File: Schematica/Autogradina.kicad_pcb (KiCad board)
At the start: 2 copper layers, 100 x 100 mm, 50 parts, among them J1 Power_Connector, J2 AC_Connector, J3 UART_Connector, J4 USB_B_Micro, J5 Boot_Jumper, J6 Ports_Connector, J7 Conn_01x02_Socket, J8 Conn_01x02_Socket, J9 Conn_01x02_Socket, K1 G5LE-1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

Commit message: Improvements
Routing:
- net 3.3V: track 0.00 -> 90.3 mm
- net N_To_Ground_Probe: track 0.00 -> 83.4 mm, vias 0 -> 2
- net Net-(U2-EN): track 0.00 -> 36.7 mm, vias 0 -> 2
- net Net-(J5-Pin_2): track 0.00 -> 18.9 mm
- net RELAY1_CONTROL: track 0.00 -> 12.1 mm, vias 0 -> 2
- net RELAY3_CONTROL: track 0.00 -> 7.98 mm
- net Net-(J4-D+): track 0.00 -> 7.47 mm
- net RELAY2_CONTROL: track 0.00 -> 7.26 mm
- net Net-(J4-D-): track 0.00 -> 7.21 mm
- net Net-(D7-A): track 7.66 -> 8.65 mm
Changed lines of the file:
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@@
   (gr_rect (start 28 27) (end 128 127)
     (stroke (width 0.1) (type default)) (fill none) (layer "Edge.Cuts"))
+  (segment (start 82.995 33.95) (end 79.405 37.54) (width 0.5) (layer "F.Cu") (net 1))
+  (segment (start 40.64 71.12) (end 33.02 63.5) (width 0.35) (layer "F.Cu") (net 1))
+  (segment (start 120.45 33.95) (end 82.995 33.95) (width 0.5) (layer "F.Cu") (net 1))
+  (segment (start 122 35.5) (end 120.45 33.95) (width 0.5) (layer "F.Cu") (net 1))
+  (segment (start 40.64 93.82) (end 40.64 71.12) (width 0.35) (layer "F.Cu") (net 1))
+  (segment (start 79.405 37.54) (end 73.08 43.865) (width 0.5) (layer "F.Cu") (net 1))
+  (segment (start 73.08 43.865) (end 73.08 47) (width 0.5) (layer "F.Cu") (net 1))
   (segment (start 63.75 28.75) (end 63.71 28.71) (width 2) (layer "F.Cu") (net 2))
   (segment (start 67 82.08) (end 70 82.08) (width 0.25) (layer "F.Cu") (net 2))
@@
   (segment (start 61 82.08) (end 64 82.08) (width 0.25) (layer "F.Cu") (net 2))
   (segment (start 89 57.08) (end 96.92 57.08) (width 2) (layer "F.Cu") (net 2))
+  (segment (start 63.75 33.25) (end 61.25 33.25) (width 0.5) (layer "F.Cu") (net 3))
+  (segment (start 62.92 41.08) (end 63 41) (width 0.5) (layer "F.Cu") (net 3))
+  (segment (start 62.92 47) (end 62.92 41.08) (width 0.5) (layer "F.Cu") (net 3))
+  (segment (start 40.52 32) (end 40.25 31.73) (width 0.5) (layer "F.Cu") (net 3))
+  (segment (start 43 32) (end 40.52 32) (width 0.5) (layer "F.Cu") (net 3))
+  (segment (start 70.25 33.25) (end 63.75 33.25) (width 0.5) (layer "F.Cu") (net 3))
+  (segment (start 61.25 33.25) (end 61 33) (width 0.5) (layer "F.Cu") (net 3))
+  (via (at 43 32) (size 0.8) (drill 0.4) (layers "F.Cu" "B.Cu") (net 3))
+  (via (at 61 33) (size 0.8) (drill 0.4) (layers "F.Cu" "B.Cu") (net 3))
+  (segment (start 44 33) (end 43 32) (width 0.5) (layer "B.Cu") (net 3))
+  (segment (start 61 33) (end 44 33) (width 0.5) (layer "B.Cu") (net 3))
   (segment (start 99 84) (end 77.7 84) (width 2) (layer "F.Cu") (net 4))
   (segment (start 112.62 95.3725) (end 112.62 89.08) (width 0.25) (layer "F.Cu") (net 4))
@@
   (segment (start 77.7 84) (end 73.7 88) (width 2) (layer "F.Cu") (net 4))
   (segment (start 121.156109 84) (end 116 84) (width 2) (layer "F.Cu") (net 4))
+  (segment (start 72.68 95.3725) (end 72.68 89.02) (width 0.35) (layer "F.Cu") (net 4))
   (segment (start 125.5 69) (end 125.5 70.19763) (width 2) (layer "F.Cu") (net 4))
   (segment (start 116 84) (end 99 84) (width 2) (layer "F.Cu") (net 4))
-  (segment (start 93 88.7) (end 93.7 88) (width 0.25) (layer "F.Cu") (net 4))
+  (segment (start 72.68 89.02) (end 73.7 88) (width 0.35) (layer "F.Cu") (net 4))
   (segment (start 125.5 60.03763) (end 125.5 65.11763) (width 2) (layer "F.Cu") (net 4))
   (segment (start 112.62 89.08) (end 113.7 88) (width 0.25) (layer "F.Cu") (net 4))
   (segment (start 113.7 86.3) (end 113.7 88) (width 2) (layer "F.Cu") (net 4))
-  (segment (start 93 95.3725) (end 93 88.7) (width 0.25) (layer "F.Cu") (net 4))
   (segment (start 125.5 75.27763) (end 123.07763 77.7) (width 2) (layer "F.Cu") (net 4))
   (segment (start 93.7 94.6725) (end 93 95.3725) (width 0.25) (layer "F.Cu") (net 4))
@@
   (segment (start 125.5 65.11763) (end 125.5 69) (width 2) (layer "F.Cu") (net 4))
   (segment (start 125.5 35.5) (end 125.5 53.88) (width 2) (layer "F.Cu") (net 4))
-  (segment (start 72.68 95.3725) (end 72.68 89.02) (width 0.25) (layer "F.Cu") (net 4))
   (segment (start 123.07763 67.54) (end 122 67.54) (width 2) (layer "F.Cu") (net 4))
   (segment (start 99 84) (end 97.7 84) (width 2) (layer "F.Cu") (net 4))
+  (segment (start 93 95.3725) (end 93 88.7) (width 0.35) (layer "F.Cu") (net 4))
   (segment (start 123.07763 77.7) (end 122 77.7) (width 2) (layer "F.Cu") (net 4))
   (segment (start 123.07763 72.62) (end 122 72.62) (width 2) (layer "F.Cu") (net 4))
   (segment (start 97.7 84) (end 93.7 88) (width 2) (layer "F.Cu") (net 4))
   (segment (start 113.7 94.2925) (end 112.62 95.3725) (width 0.25) (layer "F.Cu") (net 4))
-  (segment (start 72.68 89.02) (end 73.7 88) (width 0.25) (layer "F.Cu") (net 4))
   (segment (start 125.5 69) (end 125.5 75.27763) (width 2) (layer "F.Cu") (net 4))
+  (segment (start 93 88.7) (end 93.7 88) (width 0.35) (layer "F.Cu") (net 4))
   (segment (start 120.92 61) (end 122 59.92) (width 0.5) (layer "F.Cu") (net 5))
   (segment (start 113.3 61) (end 109 61) (width 0.5) (layer "F.Cu") (net 5))
@@
   (segment (start 88.01 79.37) (end 86.46 80.92) (width 0.5) (layer "B.Cu") (net 9))
   (segment (start 107 75) (end 96 75) (width 0.5) (layer "B.Cu") (net 9))
-  (segment (start 84.68 95.3725) (end 84.68 88.38) (width 0.25) (layer "F.Cu") (net 10))
+  (segment (start 84.68 88.38) (end 84.3 88) (width 0.35) (layer "F.Cu") (net 10))
   (segment (start 84.3 94.9925) (end 84.68 95.3725) (width 0.25) (layer "F.Cu") (net 10))
-  (segment (start 84.68 88.38) (end 84.3 88) (width 0.25) (layer "F.Cu") (net 10))
-  (segment (start 104.3 88) (end 104.3 94.6725) (width 0.25) (layer "F.Cu") (net 11))
+  (segment (start 84.68 95.3725) (end 84.68 88.38) (width 0.35) (layer "F.Cu") (net 10))
   (segment (start 104.3 94.6725) (end 105 95.3725) (width 0.25) (layer "F.Cu") (net 11))
+  (segment (start 105 95.3725) (end 105 88.7) (width 0.35) (layer "F.Cu") (net 11))
+  (segment (start 105 88.7) (end 104.3 88) (width 0.35) (layer "F.Cu") (net 11))
   (segment (start 124.3 88) (end 124.3 95.0525) (width 0.25) (layer "F.Cu") (net 12))
   (segment (start 124.3 95.0525) (end 124.62 95.3725) (width 0.25) (layer "F.Cu") (net 12))
@@
   (segment (start 84.75 119.57763) (end 84.75 118.5) (width 2.7) (layer "B.Cu") (net 15))
   (segment (start 104.75 119.57763) (end 104.75 118.5) (width 2.7) (layer "B.Cu") (net 15))
+  (segment (start 33.85 42.475) (end 37.278984 42.475) (width 0.35) (layer "F.Cu") (net 19))
+  (segment (start 39.233984 44.43) (end 40.25 44.43) (width 0.35) (layer "F.Cu") (net 19))
+  (segment (start 37.278984 42.475) (end 39.233984 44.43) (width 0.35) (layer "F.Cu") (net 19))
+  (segment (start 33.85 43.125) (end 37.151166 43.125) (width 0.35) (layer "F.Cu") (net 20))
+  (segment (start 39.726166 45.7) (end 40.25 45.7) (width 0.35) (layer "F.Cu") (net 20))
+  (segment (start 37.151166 43.125) (end 39.726166 45.7) (width 0.35) (layer "F.Cu") (net 20))
+  (segment (start 68.39 37.85) (end 62.15 37.85) (width 0.5) (layer "F.Cu") (net 22))
+  (segment (start 62.15 37.85) (end 59.05 40.95) (width 0.5) (layer "F.Cu") (net 22))
+  (segment (start 70 39.46) (end 68.39 37.85) (width 0.5) (layer "F.Cu") (net 22))
+  (segment (start 59 45.7) (end 57.75 45.7) (width 0.5) (layer "F.Cu") (net 22))
+  (segment (start 59.05 40.95) (end 59.05 45.65) (width 0.5) (layer "F.Cu") (net 22))
+  (segment (start 59.05 45.65) (end 59 45.7) (width 0.5) (layer "F.Cu") (net 22))
   (segment (start 72.68 107.5725) (end 72.68 109.93) (width 2.7) (layer "B.Cu") (net 23))
   (segment (start 72.68 109.93) (end 81.063941 118.313941) (width 2.7) (layer "B.Cu") (net 23))
@@
   (segment (start 74 75.92) (end 70 71.92) (width 0.5) (layer "B.Cu") (net 30))
   (segment (start 74 77) (end 74 75.92) (width 0.5) (layer "B.Cu") (net 30))
+  (segment (start 54.46 30.46) (end 57.75 30.46) (width 0.35) (layer "F.Cu") (net 35))
+  (segment (start 54 30) (end 54.46 30.46) (width 0.35) (layer "F.Cu") (net 35))
+  (segment (start 30.48 90.52) (end 31 90) (width 0.35) (layer "F.Cu") (net 35))
+  (segment (start 30.48 93.82) (end 30.48 90.52) (width 0.35) (layer "F.Cu") (net 35))
+  (via (at 54 30) (size 0.8) (drill 0.4) (layers "F.Cu" "B.Cu") (net 35))
+  (via (at 31 90) (size 0.8) (drill 0.4) (layers "F.Cu" "B.Cu") (net 35))
+  (segment (start 43.903984 30) (end 54 30) (width 0.35) (layer "B.Cu") (net 35))
+  (segment (start 37.025 83.975) (end 37.025 36.878984) (width 0.35) (layer "B.Cu") (net 35))
+  (segment (start 31 90) (end 37.025 83.975) (width 0.35) (layer "B.Cu") (net 35))
+  (segment (start 37.025 36.878984) (end 43.903984 30) (width 0.35) (layer "B.Cu") (net 35))
+  (segment (start 48.26 53.92) (end 45.825 51.485) (width 0.35) (layer "F.Cu") (net 36))
+  (segment (start 45.825 51.485) (end 45.825 46.95) (width 0.35) (layer "F.Cu") (net 36))
+  (segment (start 45.26 53.92) (end 44.555 53.215) (width 0.35) (layer "F.Cu") (net 37))
+  (segment (start 44.555 53.215) (end 44.555 46.95) (width 0.35) (layer "F.Cu") (net 37))
+  (segment (start 42.26 51.26) (end 42 51) (width 0.35) (layer "F.Cu") (net 38))
+  (segment (start 41.16 43.16) (end 40.25 43.16) (width 0.35) (layer "F.Cu") (net 38))
+  (segment (start 42 44) (end 41.16 43.16) (width 0.35) (layer "F.Cu") (net 38))
+  (segment (start 42.26 53.92) (end 42.26 51.26) (width 0.35) (layer "F.Cu") (net 38))
+  (via (at 42 51) (size 0.8) (drill 0.4) (layers "F.Cu" "B.Cu") (net 38))
+  (via (at 42 44) (size 0.8) (drill 0.4) (layers "F.Cu" "B.Cu") (net 38))
+  (segment (start 42 51) (end 42 44) (width 0.35) (layer "B.Cu") (net 38))
   (segment (start 48.365 47.95) (end 48.365 46.95) (width 0.25) (layer "F.Cu") (net 39))
   (segment (start 54.085 53.92) (end 48.365 48.2) (width 0.5) (layer "F.Cu") (net 39))

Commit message: Update
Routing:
- net Net-(D8-A): track 7.51 -> 91.0 mm
- net Net-(D7-A): track 8.65 -> 74.2 mm
- net Net-(D6-A): track 8.07 -> 57.7 mm, vias 0 -> 1
- net Net-(J3-Pin_3): track 0.00 -> 47.1 mm, vias 0 -> 2
- net Net-(J3-Pin_2): track 0.00 -> 46.1 mm, vias 0 -> 2
- net Mosfet_Port5: track 2.47 -> 36.8 mm, vias 1 -> 2
- net Net-(Q8-B): track 0.00 -> 23.5 mm
- net Net-(Q7-B): track 0.00 -> 16.4 mm
- net Net-(Q6-B): track 0.00 -> 8.83 mm
- net Mosfet_Port4: track 37.4 -> 32.5 mm
- net 12V: track 161.3 -> 159.7 mm

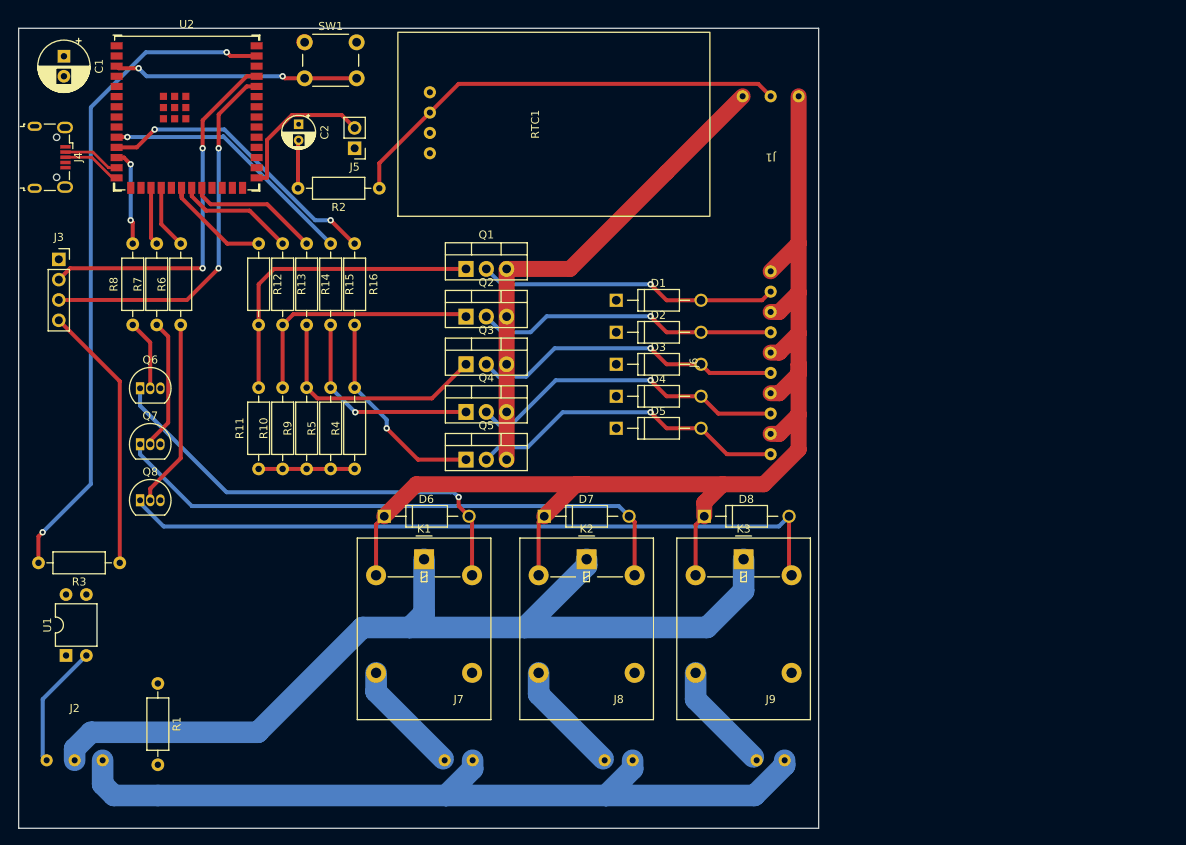
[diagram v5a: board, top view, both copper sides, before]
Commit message: Added gnd fill areas
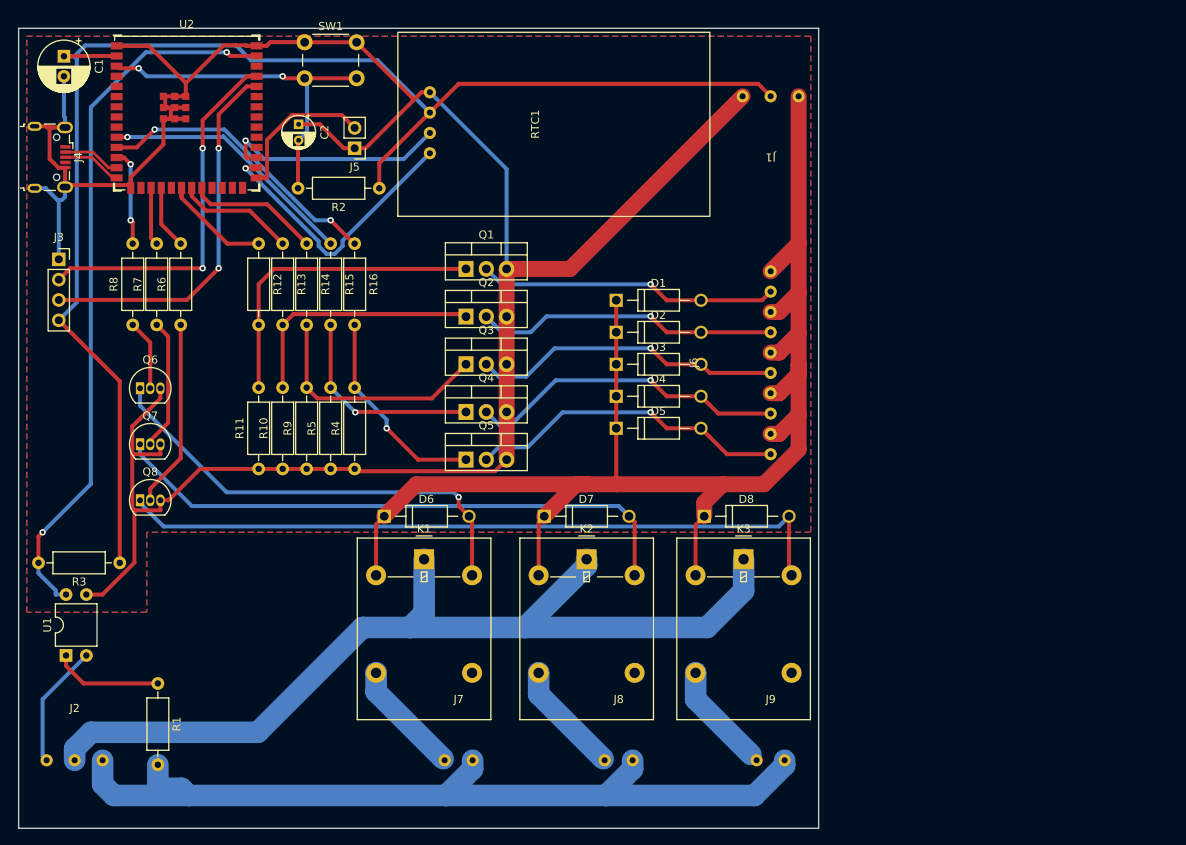
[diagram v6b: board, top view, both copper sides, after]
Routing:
- net GND: track 74.3 -> 302.9 mm
- net 3.3V: track 90.3 -> 180.7 mm
- net RTC_CLOCK: track 0.00 -> 34.8 mm, vias 0 -> 1
- net RTC_DATA: track 0.00 -> 28.8 mm, vias 0 -> 1
- net 12V: track 159.7 -> 182.8 mm
- net Net-(R1-Pad1): track 0.00 -> 13.7 mm
- net Net-(U2-EN): track 36.7 -> 45.0 mm
- net AC_N: track 102.6 -> 109.7 mm
- net N_To_Ground_Probe: track 83.4 -> 89.6 mm
- added copper zone on B.Cu, net GND
- added copper zone on F.Cu, net GND

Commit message: Finished up
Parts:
- added NT1: NetTie_2, NetTie:NetTie-2_SMD_Pad0.5mm, B.Cu at (32.5, 111.0)
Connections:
- U1 pad 2: AC_G -> Net-(NT1-Pad2)
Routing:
- net Net-(NT1-Pad2): track 0.00 -> 8.21 mm
- net AC_G: track 15.6 -> 7.71 mm
- net Net-(D7-A): track 74.2 -> 73.2 mm
- net 12V: track 182.8 -> 181.8 mm
- net Net-(D8-A): track 91.0 -> 90.3 mm
- net Net-(D6-A): track 57.7 -> 57.2 mm
- net N_To_Ground_Probe: track 89.6 -> 90.1 mm

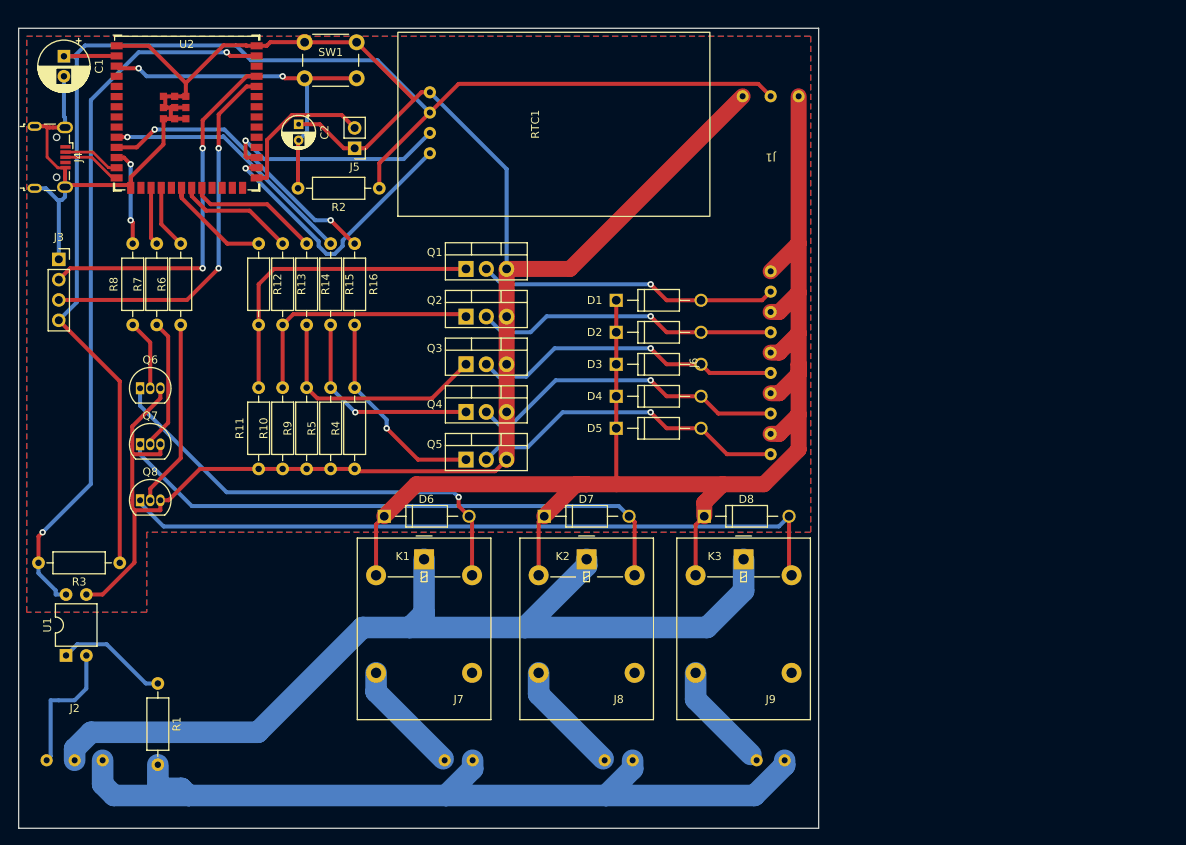
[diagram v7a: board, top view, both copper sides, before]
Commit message: Removed most of traces; Updated schematci
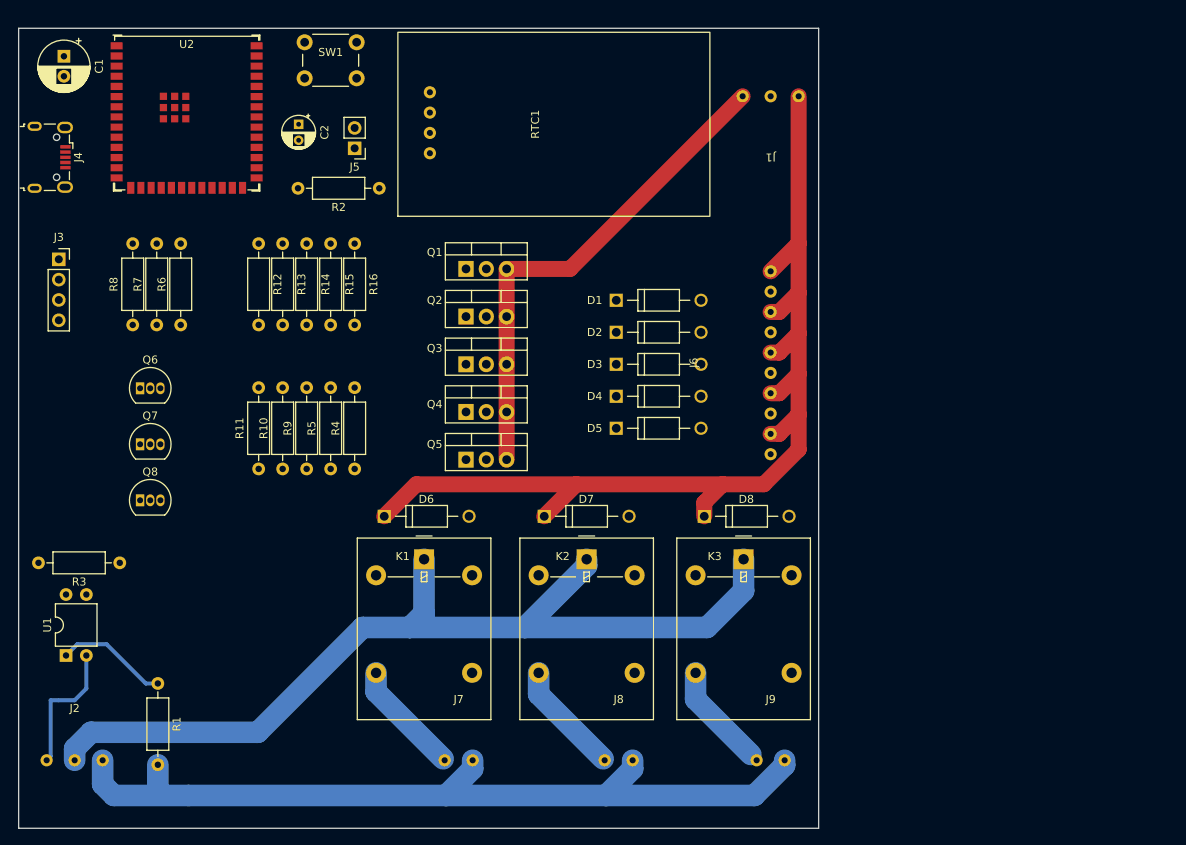
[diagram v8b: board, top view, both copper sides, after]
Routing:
- net GND: track 303.1 -> 62.3 mm
- net 3.3V: track 180.7 -> 0.00 mm
- net Net-(D8-A): track 90.3 -> 0.00 mm
- net N_To_Ground_Probe: track 90.1 -> 0.00 mm, vias 2 -> 0
- net Net-(D7-A): track 73.2 -> 0.00 mm
- net Net-(D6-A): track 57.2 -> 0.00 mm, vias 1 -> 0
- net 12V: track 181.8 -> 133.0 mm
- net Net-(J3-Pin_3): track 47.1 -> 0.00 mm, vias 2 -> 0
- net Net-(J3-Pin_2): track 46.1 -> 0.00 mm, vias 2 -> 0
- net Net-(U2-EN): track 45.0 -> 0.00 mm, vias 2 -> 0
- net Net-(D4-A): track 40.6 -> 0.00 mm, vias 1 -> 0
- net Net-(D5-A): track 40.2 -> 0.00 mm, vias 1 -> 0
- net Net-(Q1-G): track 39.6 -> 0.00 mm
- net Net-(D3-A): track 38.9 -> 0.00 mm, vias 1 -> 0
- net Net-(D2-A): track 38.0 -> 0.00 mm, vias 1 -> 0
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- removed copper zone on B.Cu, net GND
- removed copper zone on F.Cu, net GND
